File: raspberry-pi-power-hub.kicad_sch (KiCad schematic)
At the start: 0 parts

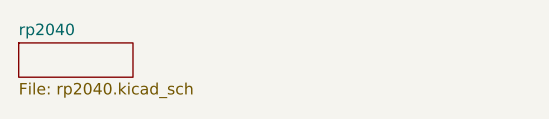
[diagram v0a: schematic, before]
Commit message: small rp2040 changes and the cypd3177
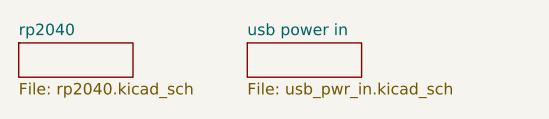
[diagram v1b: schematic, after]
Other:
- added sheet usb power in (usb_pwr_in.kicad_sch)
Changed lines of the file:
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@@
 	(paper "A4")
+	(sheet
+		(at 62.23 85.09)
+		(size 12.7 3.81)
+		(exclude_from_sim no)
+		(in_bom yes)
+		(on_board yes)
+		(dnp no)
+		(fields_autoplaced yes)
+		(stroke
+			(width 0.1524)
+			(type solid)
+		)
+		(fill
+			(color 0 0 0 0.0000)
+		)
+		(property "Sheetname" "usb power in"
+			(at 62.23 84.3784 0)
+			(effects
+				(font
+					(size 1.27 1.27)
+				)
+				(justify left bottom)
+			)
+		)
+		(property "Sheetfile" "usb_pwr_in.kicad_sch"
+			(at 62.23 89.4846 0)
+			(effects
+				(font
+					(size 1.27 1.27)
+				)
+				(justify left top)
+			)
+		)
+		(instances
+			(project "raspberry-pi-power-hub"
+				(path "/2a0acc6a-7dcb-4f06-b9d0-ff1420b61fe9"
+					(page "3")
+				)
+			)
+		)
+	)
 	(sheet
 		(at 36.83 85.09)

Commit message: finished pcb routing yay
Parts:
- added H1, H2, H3, H4: MountingHole_Pad, MountingHole:MountingHole_2.2mm_M2_Pad, symbol Mechanical:MountingHole_Pad
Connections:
- new net GND: H1.1, H2.1, H3.1, H4.1

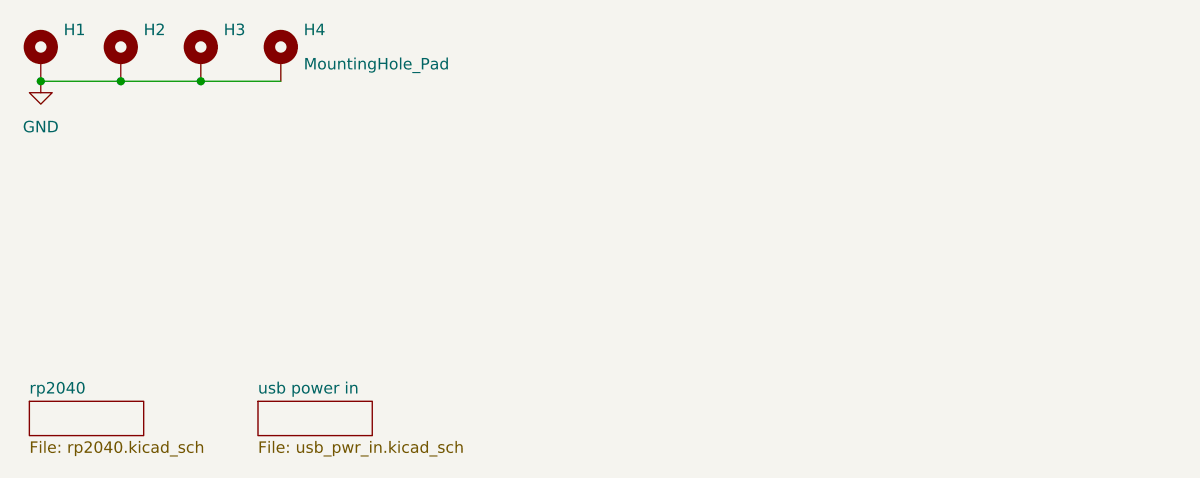
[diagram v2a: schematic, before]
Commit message: fixed via size woohoo!
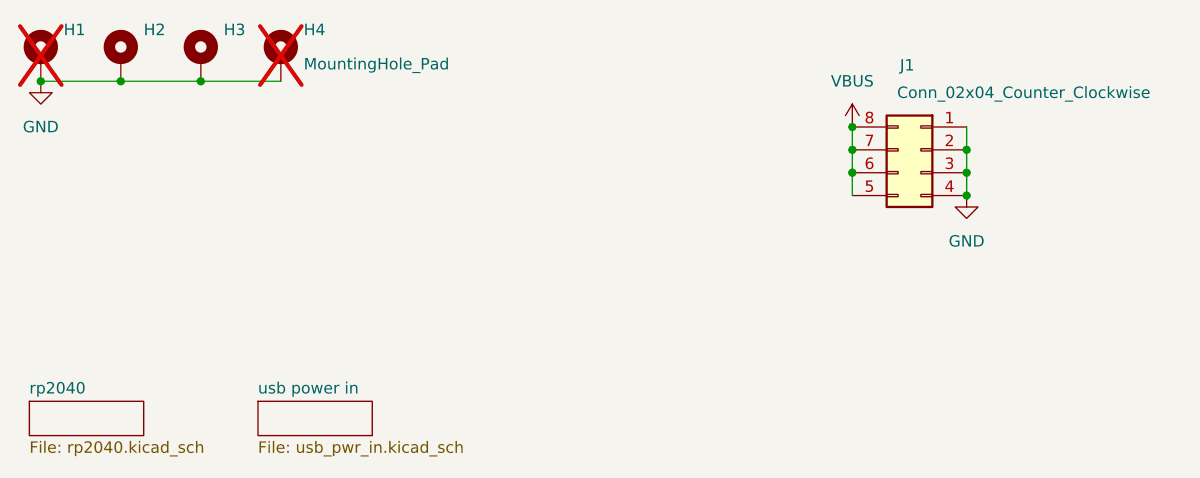
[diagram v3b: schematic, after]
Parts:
- added J1: Conn_02x04_Counter_Clockwise, Connector_PinHeader_2.54mm:PinHeader_2x04_P2.54mm_Vertical, symbol Connector_Generic:Conn_02x04_Counter_Clockwise
- H1, H4: now not fitted
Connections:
- net GND: now also J1.1 (Pin_1), J1.2 (Pin_2), J1.3 (Pin_3), J1.4 (Pin_4)
- new net VBUS: J1.5 (Pin_5), J1.6 (Pin_6), J1.7 (Pin_7), J1.8 (Pin_8)
